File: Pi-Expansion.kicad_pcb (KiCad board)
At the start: 2 copper layers, 18 parts, among them J1 RPi_GPIO, J2 SMA_H, P1 BATT, U1 A2200-A, U2 SPX2920U-5.0

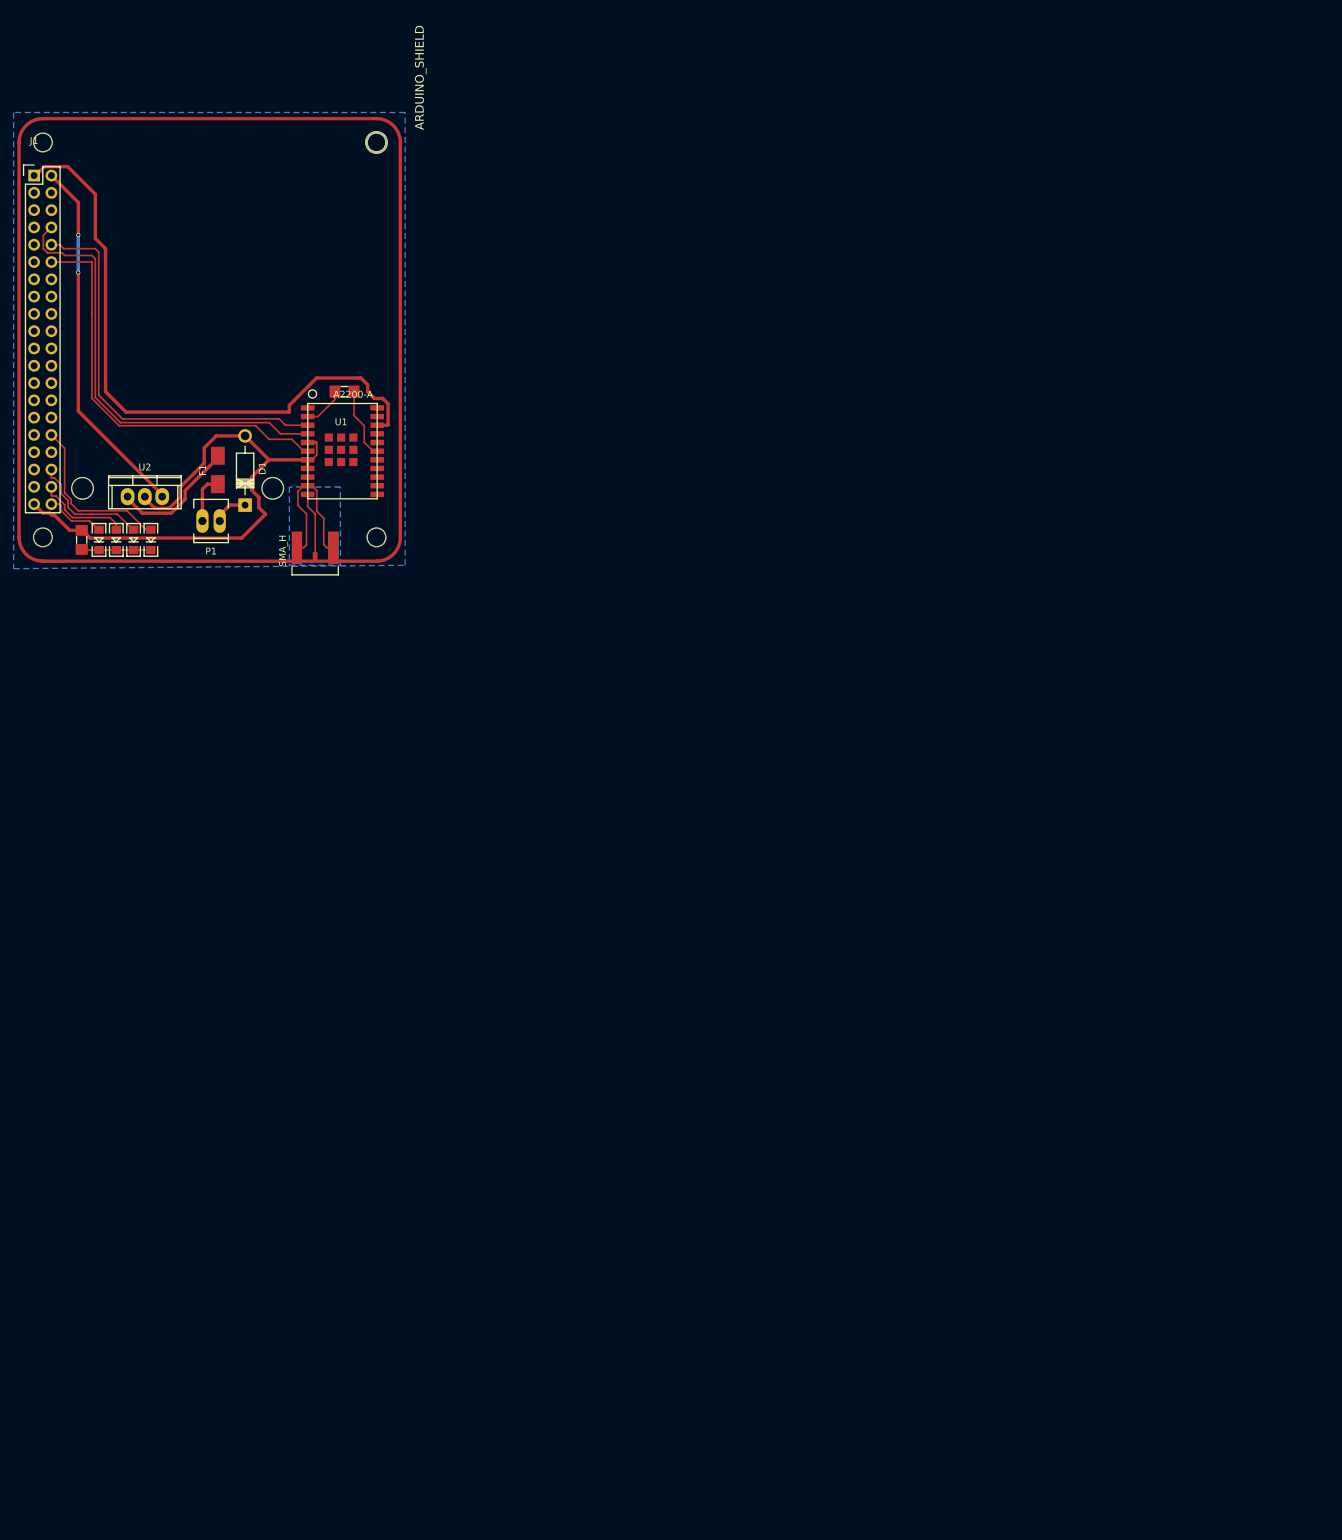
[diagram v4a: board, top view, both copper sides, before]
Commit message: minor tweaks, and rotated pi header, removed infill and traces
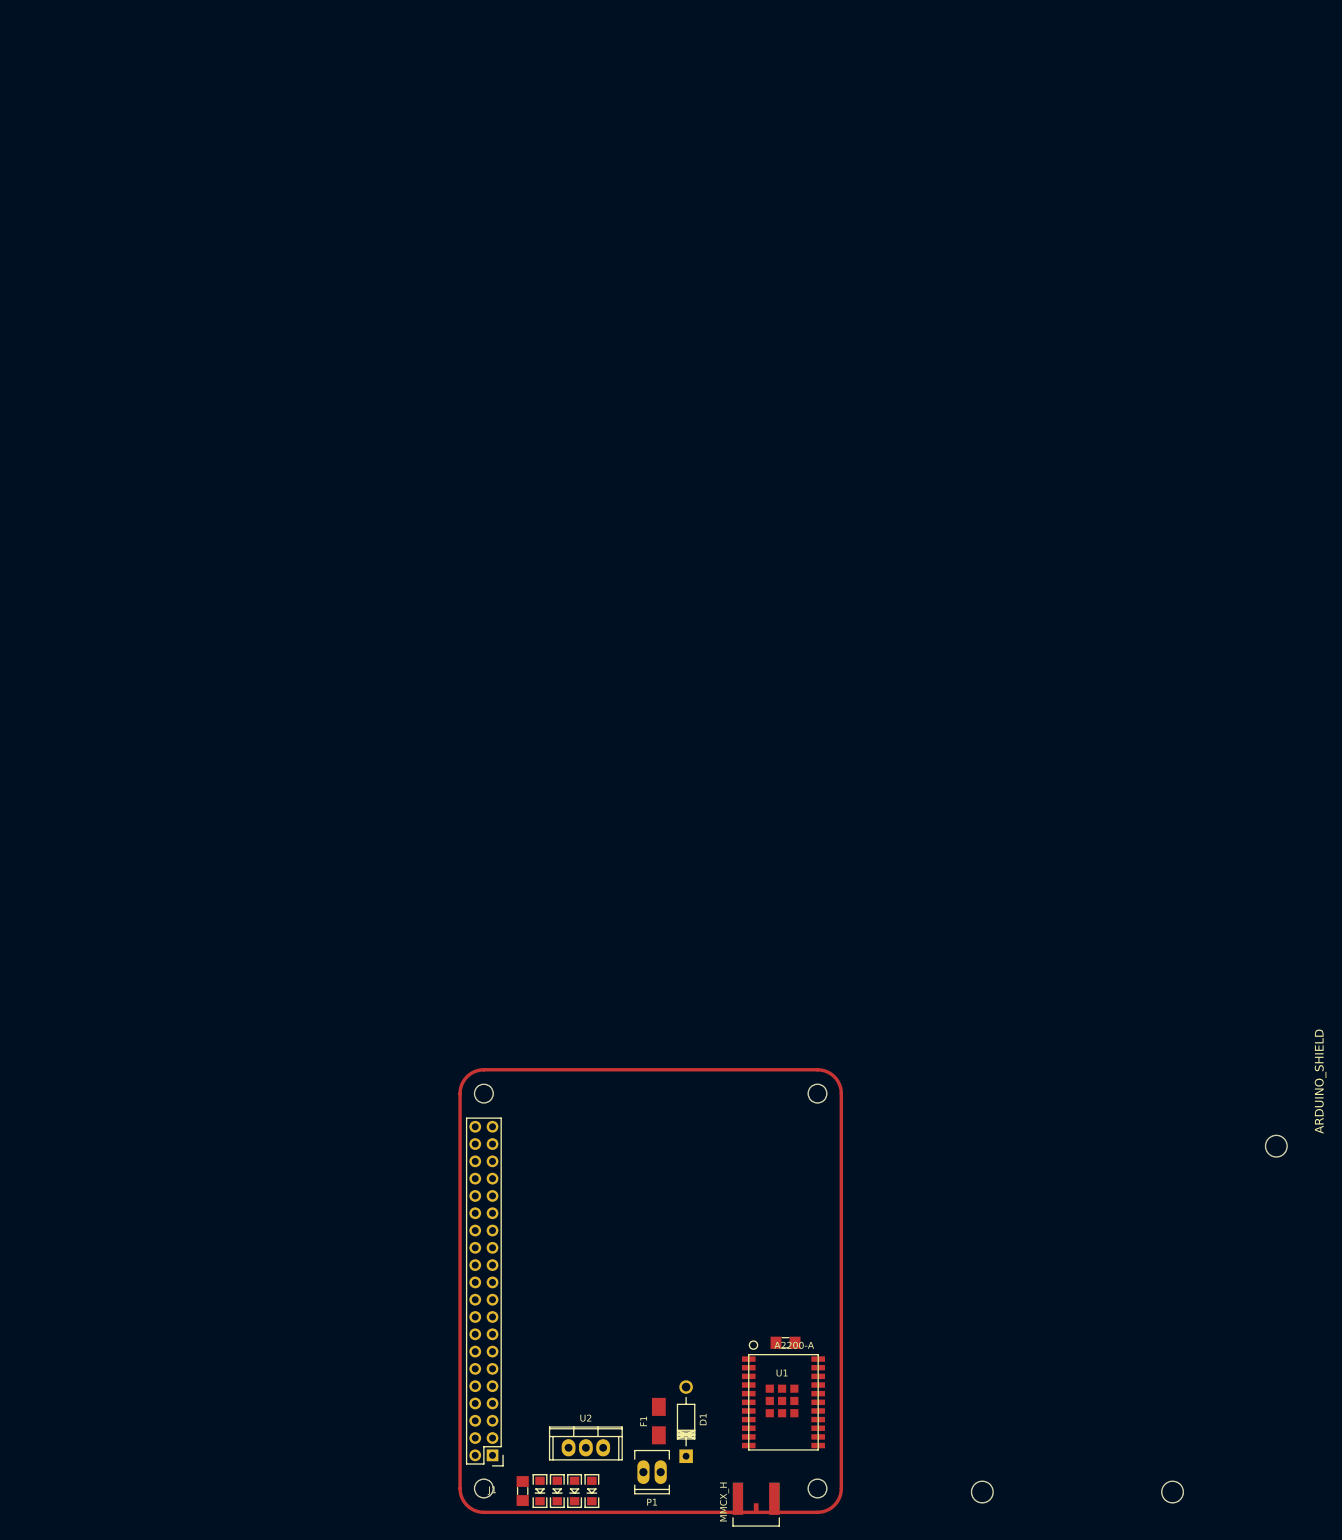
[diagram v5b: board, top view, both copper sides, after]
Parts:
- D1: value D -> DIODE_SCHOTTKY
- J2: value SMA_H -> MMCX_H
- moved J1 199.7 mm to (72.8, 129.2), turned to 180 degrees
- moved ARDUINO_SHIELD 198.0 mm to (137.2, 68.6)
- moved D1 154.0 mm to (101.3, 129.4)
- moved 1111 154.0 mm to (71.6, 134.1)
- moved 1112 154.0 mm to (71.6, 76.1)
- moved 1121 154.0 mm to (120.6, 134.1)
- moved 1122 154.0 mm to (120.6, 76.1)
- moved F1 154.0 mm to (97.3, 124.2)
- moved J2 154.0 mm to (111.6, 135.6)
- moved LED1 154.0 mm to (87.4, 134.5)
- moved LED2 154.0 mm to (84.9, 134.5)
- moved LED3 154.0 mm to (82.3, 134.5)
- moved LED4 154.0 mm to (79.8, 134.5)
- moved P1 154.0 mm to (96.3, 131.7)
- moved R1 154.0 mm to (115.9, 112.7)
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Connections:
- D1 pad 1: Net-(D1-Pad1) -> (no net)
- D1 pad 2: GND -> (no net)
- J1 pad 11: Net-(J1-Pad11) -> (no net)
- J1 pad 12: GPS_WAKE -> (no net)
- J1 pad 13: Net-(J1-Pad13) -> (no net)
- J1 pad 14: Net-(J1-Pad14) -> GND
- J1 pad 15: Net-(J1-Pad15) -> (no net)
- J1 pad 16: Net-(J1-Pad16) -> (no net)
- J1 pad 17: Net-(J1-Pad17) -> +3V3
- J1 pad 18: Net-(J1-Pad18) -> (no net)
- J1 pad 19: Net-(J1-Pad19) -> (no net)
- J1 pad 20: Net-(J1-Pad20) -> GND
- J1 pad 21: Net-(J1-Pad21) -> (no net)
- J1 pad 22: Net-(J1-Pad22) -> (no net)
- J1 pad 23: Net-(J1-Pad23) -> (no net)
- J1 pad 24: Net-(J1-Pad24) -> (no net)
- J1 pad 25: Net-(J1-Pad25) -> GND
- J1 pad 26: Net-(J1-Pad26) -> (no net)
- J1 pad 27: Net-(J1-Pad27) -> (no net)
- J1 pad 28: Net-(J1-Pad28) -> (no net)
- J1 pad 29: Net-(J1-Pad29) -> (no net)
- J1 pad 3: Net-(J1-Pad3) -> (no net)
- J1 pad 30: Net-(J1-Pad30) -> GND
- J1 pad 31: Net-(J1-Pad31) -> (no net)
- J1 pad 33: Net-(J1-Pad33) -> (no net)
- J1 pad 34: Net-(J1-Pad34) -> GND
- J1 pad 35: Net-(J1-Pad35) -> (no net)
- J1 pad 37: Net-(J1-Pad37) -> (no net)
- J1 pad 4: Net-(J1-Pad4) -> +5V
- J1 pad 5: Net-(J1-Pad5) -> (no net)
- J1 pad 6: Net-(J1-Pad6) -> (no net)
- J1 pad 7: Net-(J1-Pad7) -> (no net)
- J1 pad 9: Net-(J1-Pad9) -> GND
- P1 pad 1: Net-(D1-Pad1) -> (no net)
- R1 pad 2: Net-(R1-Pad2) -> Vout-1v8
- U1 pad 1: Net-(U1-Pad1) -> (no net)
- U1 pad 12: Net-(U1-Pad12) -> (no net)
- U1 pad 13: Net-(U1-Pad13) -> (no net)
- U1 pad 14: Net-(U1-Pad14) -> (no net)
- U1 pad 15: Net-(U1-Pad15) -> (no net)
- U1 pad 16: Net-(U1-Pad16) -> (no net)
- U1 pad 17: Net-(R1-Pad2) -> Net-(R1-Pad1)
- U1 pad 18: Net-(U1-Pad18) -> (no net)
- U1 pad 19: GND -> Net-(U1-Pad19)
- U1 pad 2: Net-(R1-Pad1) -> Vout-1v8
- U1 pad 21: Net-(U1-Pad21) -> (no net)
- U1 pad 22: Net-(U1-Pad22) -> GND
- U1 pad 6: GPS_WAKE -> Net-(U1-Pad19)
- U1 pad 9: Net-(U1-Pad9) -> (no net)
- U2 pad 3: +5V -> (no net)
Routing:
- net +3V3: track 93.8 -> 0.00 mm
- net GND: track 86.7 -> 0.00 mm
- net GPS_RX: track 65.6 -> 0.00 mm
- net GPS_TX: track 60.9 -> 0.00 mm
- net GPS_WAKE: track 60.9 -> 0.00 mm
- net +5V: track 53.9 -> 0.00 mm, vias 2 -> 0
- net PI_LED_1: track 24.6 -> 0.00 mm
- net Net-(J2-Pad2): track 23.3 -> 0.00 mm
- net Net-(F1-Pad2): track 18.8 -> 0.00 mm
- net PI_LED_2: track 17.8 -> 0.00 mm
- net PI_LED_3: track 13.8 -> 0.00 mm
- net Net-(R1-Pad2): track 10.5 -> 0.00 mm
- net Net-(LED1-PadK): track 10.2 -> 0.00 mm
- net Net-(J2-Pad1): track 9.67 -> 0.00 mm
- net PI_LED_4: track 8.98 -> 0.00 mm
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- removed copper zone on B.Cu, net GND
- removed copper zone on B.Cu, net Net-(J2-Pad2)

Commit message: Made minor tweaks to schematic layout, updated footprints and  tweaked pcb layout
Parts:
- removed D1: DIODE_SCHOTTKY, Diodes_ThroughHole:Diode_DO-41_SOD81_Horizontal_RM10
- removed J2: MMCX_H, SMA_H
- moved ARDUINO_SHIELD 67.7 mm to (69.8, 61.0)
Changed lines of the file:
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@@
 (kicad_pcb (version 4) (host pcbnew 4.0.2-1.fc23-product)
   (general
-    (links 35)
-    (no_connects 35)
-    (area 0 0 0 0)
+    (links 30)
+    (no_connects 30)
+    (area 67.819999 64.472029 195.7292 139.863031)
     (thickness 1.6)
     (drawings 8)
     (tracks 0)
     (zones 0)
-    (modules 18)
+    (modules 16)
     (nets 18)
   )
@@
     (mod_text_size 1 1)
     (mod_text_width 0.15)
-    (pad_size 1.5 1.5)
-    (pad_drill 0.6)
+    (pad_size 3.175 3.175)
+    (pad_drill 3.175)
     (pad_to_mask_clearance 0)
     (aux_axis_origin 0 0)
@@
     (add_net "Net-(F1-Pad2)")
   )
-  (module Diodes_ThroughHole:Diode_DO-41_SOD81_Horizontal_RM10 (layer F.Cu)
-    (at 101.27254 129.36 90)
-    (descr "Diode, DO-41, SOD81, Horizontal, RM 10mm,")
-    (tags "Diode, DO-41, SOD81, Horizontal, RM 10mm, 1N4007, SB140,")
-    (fp_text reference D1 (at 5.38734 2.53746 90) (layer F.SilkS)
-      (effects (font (size 1 1) (thickness 0.15)))
-    )
-    (fp_text value DIODE_SCHOTTKY (at 4.37134 -3.55854 90) (layer F.Fab)
-      (effects (font (size 1 1) (thickness 0.15)))
-    )
-    (fp_line (start 7.62 -0.00254) (end 8.636 -0.00254) (layer F.SilkS) (width 0.15))
-    (fp_line (start 2.794 -0.00254) (end 1.524 -0.00254) (layer F.SilkS) (width 0.15))
-    (fp_line (start 3.048 -1.27254) (end 3.048 1.26746) (layer F.SilkS) (width 0.15))
-    (fp_line (start 3.302 -1.27254) (end 3.302 1.26746) (layer F.SilkS) (width 0.15))
-    (fp_line (start 3.556 -1.27254) (end 3.556 1.26746) (layer F.SilkS) (width 0.15))
-    (fp_line (start 2.794 -1.27254) (end 2.794 1.26746) (layer F.SilkS) (width 0.15))
-    (fp_line (start 3.81 -1.27254) (end 2.54 1.26746) (layer F.SilkS) (width 0.15))
-    (fp_line (start 2.54 -1.27254) (end 3.81 1.26746) (layer F.SilkS) (width 0.15))
-    (fp_line (start 3.81 -1.27254) (end 3.81 1.26746) (layer F.SilkS) (width 0.15))
-    (fp_line (start 3.175 -1.27254) (end 3.175 1.26746) (layer F.SilkS) (width 0.15))
-    (fp_line (start 2.54 1.26746) (end 2.54 -1.27254) (layer F.SilkS) (width 0.15))
-    (fp_line (start 2.54 -1.27254) (end 7.62 -1.27254) (layer F.SilkS) (width 0.15))
-    (fp_line (start 7.62 -1.27254) (end 7.62 1.26746) (layer F.SilkS) (width 0.15))
-    (fp_line (start 7.62 1.26746) (end 2.54 1.26746) (layer F.SilkS) (width 0.15))
-    (pad 2 thru_hole circle (at 10.16 -0.00254 270) (size 1.99898 1.99898) (drill 1.27) (layers *.Cu *.Mask F.SilkS))
-    (pad 1 thru_hole rect (at 0 -0.00254 270) (size 1.99898 1.99898) (drill 1.00076) (layers *.Cu *.Mask F.SilkS))
-  )
   (module Sailbot_Custom:ARDUINO_SHIELD_3_HOLE (layer F.Cu)
-    (at 137.16 68.58 270)
+    (at 69.85 60.96 270)
     (descr http://www.thingiverse.com/thing:9630)
     (fp_text reference ARDUINO_SHIELD (at 5.715 -57.15 270) (layer F.SilkS)
@@
     )
   )
-  (module SMA_H (layer F.Cu)
-    (at 111.56 135.613 270)
-    (attr smd)
-    (fp_text reference J2 (at -0.05 -4.65 270) (layer F.SilkS) hide
-      (effects (font (size 1 1) (thickness 0.2)))
-    )
-    (fp_text value MMCX_H (at 0.47 4.76 270) (layer F.SilkS)
-      (effects (font (size 1 1) (thickness 0.2)))
-    )
-    (fp_line (start 4.0005 -3.40106) (end 4.0005 3.40106) (layer F.SilkS) (width 0.09906))
-    (fp_line (start 4.0005 3.40106) (end 2.79908 3.40106) (layer F.SilkS) (width 0.09906))
-    (fp_line (start 2.79908 -3.40106) (end 3.99796 -3.40106) (layer F.SilkS) (width 0.09906))
-    (pad 3 smd rect (at 0 -2.67208 270) (size 4.69646 1.49606) (layers F.Cu F.Paste F.Mask)
-      (net 10 "Net-(J2-Pad2)") (clearance 0.19558))
-    (pad 4 smd rect (at 0 2.67208 270) (size 4.69646 1.49606) (layers B.Cu B.Paste B.Mask)
-      (net 10 "Net-(J2-Pad2)") (clearance 0.19558))
-    (pad 2 smd rect (at 0 2.67208 270) (size 4.69646 1.49606) (layers F.Cu F.Paste F.Mask)
-      (net 10 "Net-(J2-Pad2)") (clearance 0.19558))
-    (pad 5 smd rect (at 0 -2.67208 270) (size 4.69646 1.49606) (layers B.Cu B.Paste B.Mask)
-      (net 10 "Net-(J2-Pad2)") (clearance 0.19558))
-    (pad 1 smd rect (at 1.397 0 270) (size 1.49606 0.6985) (layers F.Cu F.Paste F.Mask)
-      (net 11 "Net-(J2-Pad1)") (clearance 0.19558))
-    (model ../../../../../home/whogg/Documents/OpenSCAD/SMA_CONNECTOR/SMA_CONNECTOR.wrl
-      (at (xyz 0 0 0))
-      (scale (xyz 0.3937 0.3937 0.3937))
-      (rotate (xyz 270 0 0))
-    )
-  )

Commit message: First draft pcb layout, most tracks in place, footprints in near final positions
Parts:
- added D1: DIODE_SCHOTTKY, FT:DIODE_SOD-323, F.Cu at (99.1, 125.7)
- added D2: DIODE_SCHOTTKY, FT:DIODE_SOD-323, F.Cu at (101.6, 125.7)
- added J2: MMCX_H, Universal:MMCX_V, F.Cu at (109.2, 133.3)
- added R3: 2.2k, FT:1206, F.Cu at (111.8, 110.5)
- added R4: 2.2k, FT:1206, F.Cu at (114.3, 110.5)
- U2: footprint Power_Integrations:TO-220 -> Converters_DCDC_ACDC:DCDC-Conv_Recom_R-78HBxx-0.5
- moved ARDUINO_SHIELD 707.1 mm to (569.9, 561.0)
- moved U2 11.5 mm to (95.2, 120.7)
- moved P1 4.16 mm to (100.3, 130.8)
- moved F1 3.45 mm to (95.2, 127.0)
- moved R1 2.41 mm to (116.8, 110.5), turned to 90 degrees
- moved LED2 2.41 mm to (86.4, 132.6)
- moved LED3 2.41 mm to (83.9, 132.6)
- moved LED4 2.41 mm to (81.3, 132.6)
- moved R2 2.41 mm to (78.8, 132.6)
- moved LED1 2.41 mm to (89.0, 132.6)
- moved U1 1.27 mm to (114.3, 121.9)
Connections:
- J1 pad 6: (no net) -> GND
- P1 pad 1: (no net) -> Net-(D1-PadK)
- U1 pad 15: (no net) -> Net-(R3-Pad1)
- U1 pad 16: (no net) -> Net-(R4-Pad1)
- U1 pad 22: GND -> +3V3
- U1 pad 7: GND -> Net-(U1-Pad7)
- U1 pad 8: GND -> Net-(U1-Pad7)
- U2 pad 3: (no net) -> Net-(D2-PadA)
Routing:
- net +3V3: track 0.00 -> 77.3 mm
- net +5V: track 0.00 -> 50.9 mm
- net GPS_TX: track 0.00 -> 41.3 mm
- net GPS_RX: track 0.00 -> 40.8 mm
- net GND: track 0.00 -> 20.9 mm, vias 0 -> 1
- net Net-(J2-Pad2): track 0.00 -> 19.7 mm
- net Net-(R3-Pad1): track 0.00 -> 18.7 mm
- net Vout-1v8: track 0.00 -> 17.4 mm
- net Net-(R4-Pad1): track 0.00 -> 15.0 mm
- net Net-(R1-Pad1): track 0.00 -> 12.0 mm
- net Net-(LED1-PadK): track 0.00 -> 10.9 mm
- net Net-(D2-PadA): track 0.00 -> 6.38 mm
- net Net-(D1-PadK): track 0.00 -> 4.98 mm
- net Net-(J2-Pad1): track 0.00 -> 4.95 mm
- net Net-(F1-Pad1): track 0.00 -> 4.52 mm
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
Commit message: Final Layout, Traces and footprints in place, added GPS_TX sensing circuit 3.3v powerled.
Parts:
- added J3: PINHEADER_2X2_SMD, Sailbot_Custom:2-WAY-SMD-JUMPER, F.Cu at (109.0, 111.9)
- added JP1: M02X02, Sockets_MOLEX_KK-System:Socket_MOLEX-KK-RM2-54mm_Lock_4pin_straight, F.Cu at (95.3, 133.4)
- added LED5: LED, FT:LED-1206, F.Cu at (88.0, 133.5)
- added LED6: LED, FT:LED-1206, F.Cu at (86.0, 133.5)
- added Q1: Q_NPN_BCE, TO_SOT_Packages_SMD:SOT-23, F.Cu at (88.0, 129.0)
- added R5: 2.2, Resistors_SMD:R_1206, F.Cu at (88.9, 124.0)
- moved ARDUINO_SHIELD 707.1 mm to (69.8, 61.0)
- moved LED1 11.0 mm to (78.0, 133.5)
- moved R2 7.33 mm to (80.6, 125.5)
- moved LED2 6.48 mm to (80.0, 133.5)
- moved P1 4.02 mm to (103.4, 133.4)
- moved LED4 2.80 mm to (84.0, 133.5)
- moved LED3 2.08 mm to (82.0, 133.5)
- moved F1 0.80 mm to (95.3, 126.2)
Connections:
- J1 pad 11: (no net) -> ON_OFF
- J1 pad 12: (no net) -> WAKEUP
- J1 pad 13: (no net) -> PI_LED_1
- J1 pad 15: (no net) -> PI_LED_2
- J1 pad 16: (no net) -> PI_LED_3
- J1 pad 18: (no net) -> PI_LED_4
- J1 pad 3: (no net) -> Net-(J1-Pad3)
- J1 pad 32: PI_LED_1 -> (no net)
- J1 pad 36: PI_LED_2 -> (no net)
- J1 pad 38: PI_LED_3 -> (no net)
- J1 pad 40: PI_LED_4 -> (no net)
- J1 pad 5: (no net) -> Net-(J1-Pad5)
- U1 pad 19: Net-(U1-Pad19) -> Net-(J3-Pad4)
- U1 pad 6: Net-(U1-Pad19) -> Net-(J3-Pad2)
- U1 pad 7: Net-(U1-Pad7) -> GND
- U1 pad 8: Net-(U1-Pad7) -> GND
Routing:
- net WAKEUP: track 0.00 -> 70.2 mm, vias 0 -> 1
- net ON_OFF: track 0.00 -> 68.1 mm
- net +3V3: track 77.3 -> 116.4 mm, vias 0 -> 2
- net Net-(J1-Pad5): track 0.00 -> 32.6 mm
- net PI_LED_4: track 0.00 -> 30.4 mm, vias 0 -> 1
- net Net-(J1-Pad3): track 0.00 -> 29.1 mm
- net PI_LED_3: track 0.00 -> 27.4 mm, vias 0 -> 2
- net PI_LED_2: track 0.00 -> 23.6 mm, vias 0 -> 1
- net PI_LED_1: track 0.00 -> 22.6 mm, vias 0 -> 1
- net Net-(J3-Pad4): track 0.00 -> 18.8 mm, vias 0 -> 2
- net GPS_TX: track 41.3 -> 57.7 mm, vias 0 -> 2
- net Net-(J3-Pad2): track 0.00 -> 12.6 mm
- net Net-(LED1-PadK): track 10.9 -> 21.1 mm
- net GND: track 20.9 -> 30.6 mm
- net Vout-1v8: track 17.4 -> 24.0 mm
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- added copper zone on F.Cu, net GND
- added copper zone on B.Cu, net Net-(J2-Pad2)
